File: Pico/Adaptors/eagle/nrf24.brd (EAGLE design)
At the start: 17.4 x 15.2 mm, 4 parts, among them IC1 LD117AS33TR

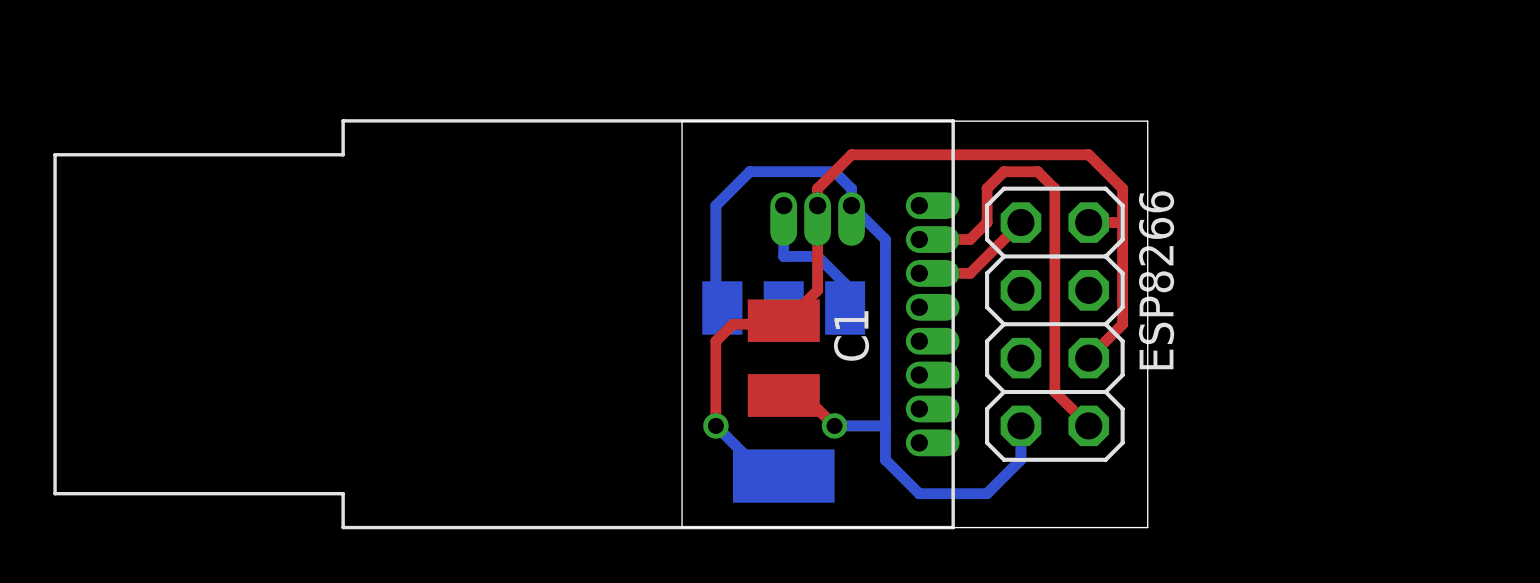
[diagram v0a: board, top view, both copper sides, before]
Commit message: nrf24 adaptor, and DRC
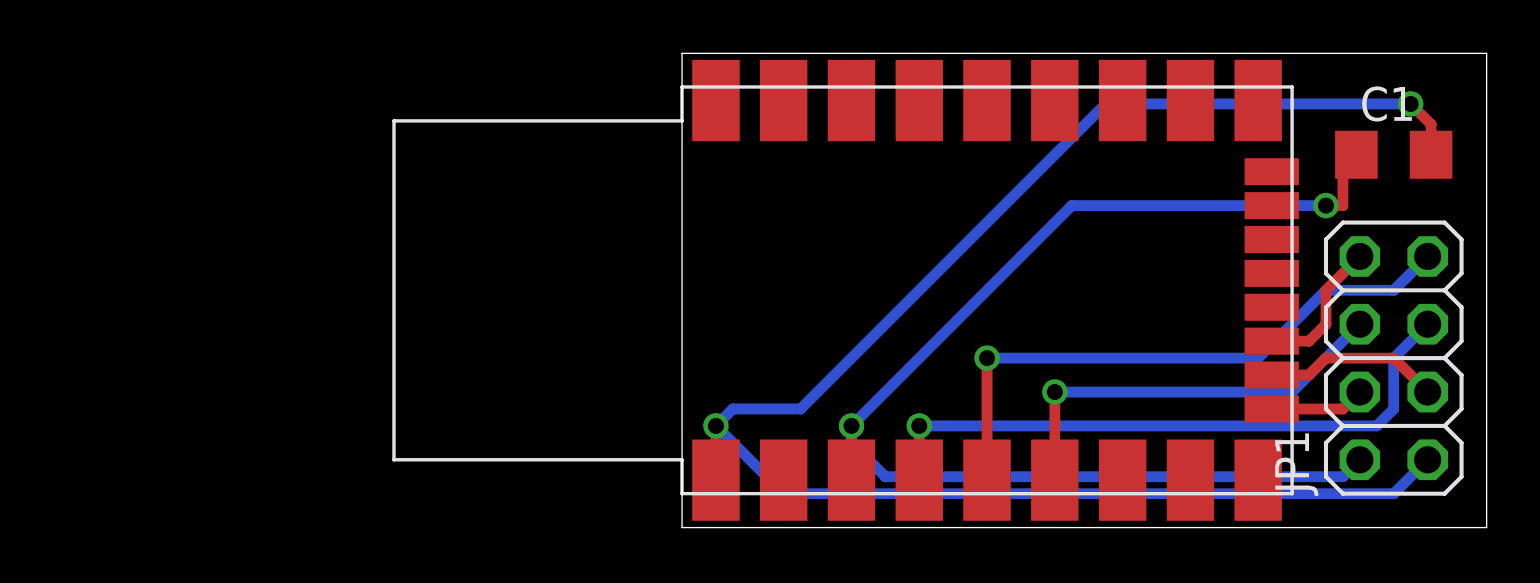
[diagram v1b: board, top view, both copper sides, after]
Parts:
- removed ESP8266: (no value), pinhead:2X04
- removed IC1: LD117AS33TR, v-reg:SOT223
- added JP1: (no value), pinhead:2X04
- C1: device rcl:C1210 -> rcl:C1206
- U$1: value ESPRUINO_PICO_0.05 -> ESPRUINO_PICO_SMDONLY; device espruino_pico:ESPRUINO_PICO_0.05 -> espruino_pico:ESPRUINO_PICO_SMDONLY
- moved C1 24.1 mm to (26.7, 14.0), turned to 0 degrees
- moved U$1 12.8 mm to (15.2, 8.89)
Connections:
- removed net ESP_RX: ESP8266.1, U$1.A2
- removed net ESP_TX: ESP8266.8, U$1.A3
- removed net GND: C1.2, ESP8266.7, IC1.1, U$1.GND_2
- removed net VCC: C1.1, ESP8266.2, ESP8266.6, IC1.4, U$1.3.3V_2
- new net N$2: C1.2, JP1.1, U$1.GND
- new net N$4: JP1.5, U$1.B3
- new net N$5: JP1.7, U$1.B4
- new net N$6: JP1.6, U$1.B5
- new net N$7: JP1.4, U$1.B8
- new net N$8: JP1.3, U$1.B9
- new net N$9: JP1.8, U$1.A10
- net N$1: now also C1.1, JP1.2, U$1.3.3V; no longer IC1.3, U$1.5V_2
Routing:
- net N$2: track 0.00 -> 63.5 mm, vias 0 -> 2
- net N$1: track 5.53 -> 46.5 mm, vias 0 -> 2
- net VCC: track 35.5 -> 0.00 mm, vias 1 -> 0
- net GND: track 32.2 -> 0.00 mm, vias 1 -> 0
- net N$4: track 0.00 -> 23.8 mm, vias 0 -> 1
- net N$5: track 0.00 -> 22.7 mm, vias 0 -> 1
- net ESP_TX: track 16.6 -> 0.00 mm
- net N$6: track 0.00 -> 15.8 mm, vias 0 -> 1
- net N$8: track 0.00 -> 6.63 mm
- net N$9: track 0.00 -> 5.36 mm
- net ESP_RX: track 4.60 -> 0.00 mm
- net N$7: track 0.00 -> 3.57 mm
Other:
- board size 17.4 x 15.2 mm -> 30.1 x 17.8 mm
